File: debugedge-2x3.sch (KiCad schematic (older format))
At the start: 2 parts, among them J1 Conn_ARM_JTAG_SWD_10, J2 DebugEdge_02x03

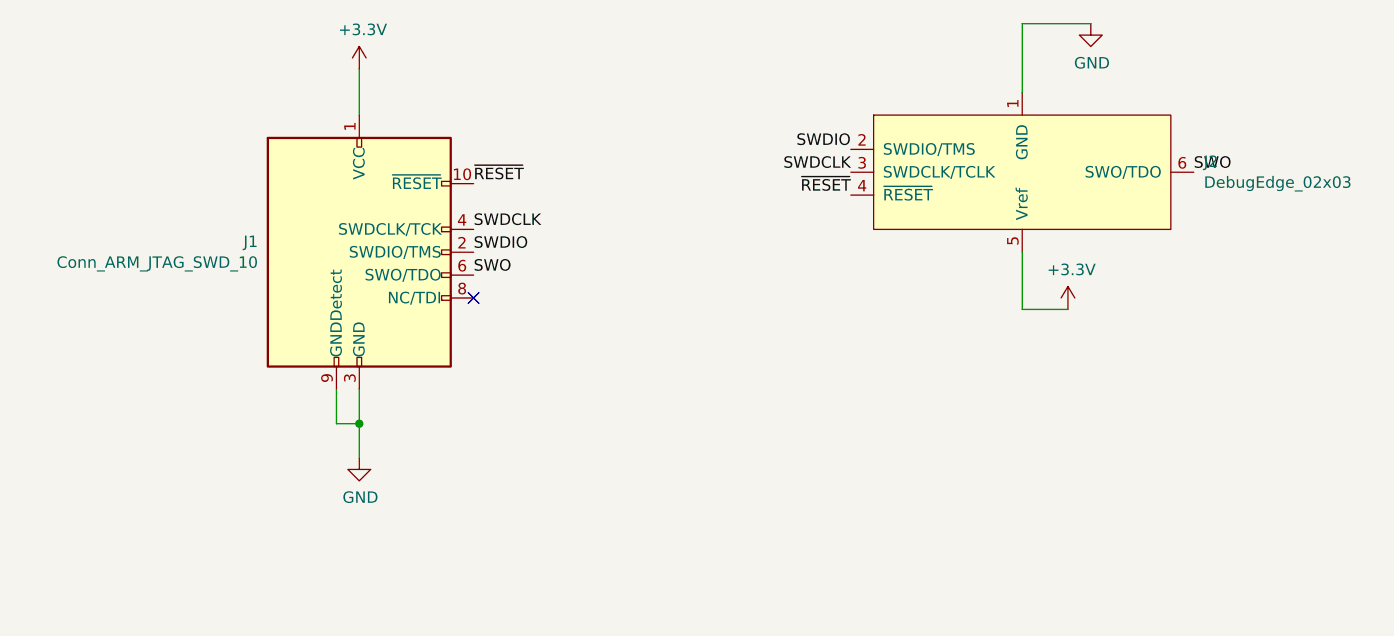
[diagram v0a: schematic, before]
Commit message: fix wrong connector
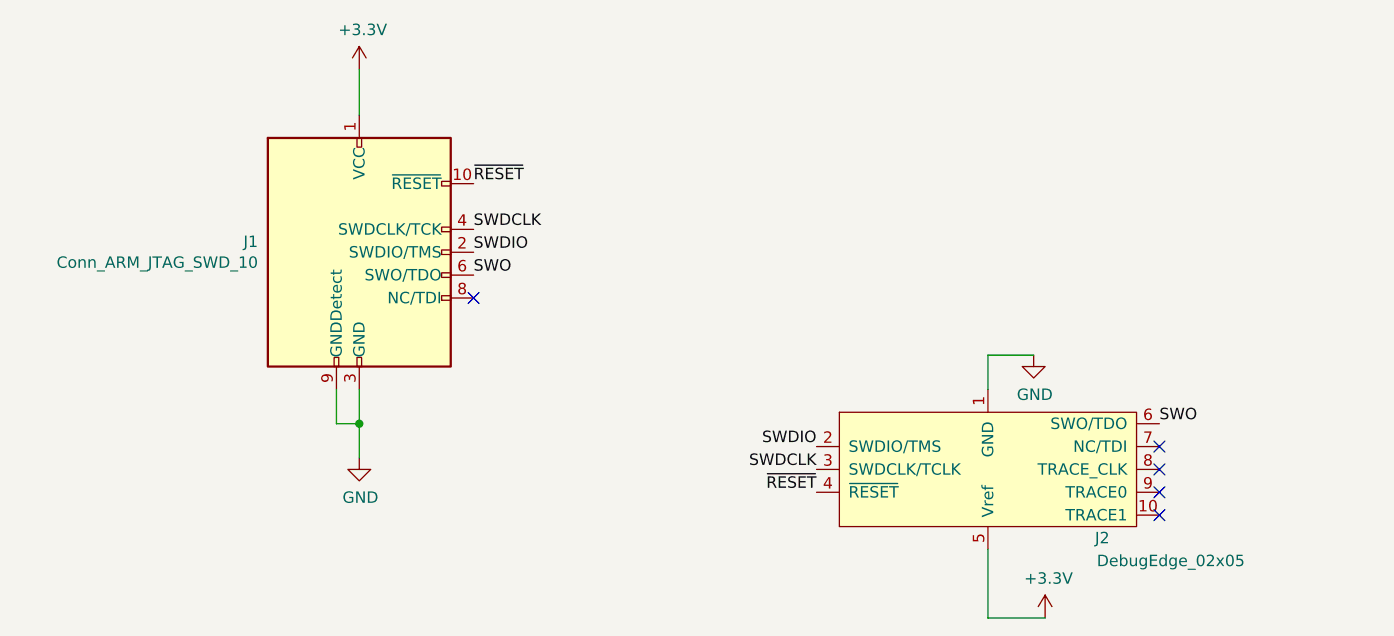
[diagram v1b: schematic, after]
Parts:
- removed J2: DebugEdge_02x03, Connector_DebugEdge:DebugEdge_2x03_Target, symbol Connector_DebugEdge:DebugEdge_02x03
- added J2: DebugEdge_02x05, Connector_DebugEdge:DebugEdge_2x05_Host, symbol Connector_DebugEdge:DebugEdge_02x05
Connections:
- net +3V3: now also J2.5 (Vref)
- net GND: now also J2.1 (GND)
- net SWDCLK: now also J2.3 (SWDCLK/TCLK)
- net SWDIO: now also J2.2 (SWDIO/TMS)
- net SWO: now also J2.6 (SWO/TDO)
- net ~RESET: now also J2.4 (~RESET~)
- no-connect marks 1 -> 5
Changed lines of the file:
@@
-$EndComp
-$Comp
-L Connector_DebugEdge:DebugEdge_02x03 J2
-U 1 1 5FF7E7FA
-P 5100 2450
-F 0 "J2" H 5894 2496 50  0000 L CNN
-F 1 "DebugEdge_02x03" H 5894 2405 50  0000 L CNN
-F 2 "Connector_DebugEdge:DebugEdge_2x03_Target" H 5100 2850 50  0001 C CNN
-F 3 "" H 5100 2850 50  0001 C CNN
-	1    5100 2450
-	1    0    0    -1
 $EndComp
 $Comp
 L power:GND #PWR0101
 U 1 1 5FF7F2E3
-P 5400 1800
-F 0 "#PWR0101" H 5400 1550 50  0001 C CNN
-F 1 "GND" H 5405 1627 50  0000 C CNN
-F 2 "" H 5400 1800 50  0001 C CNN
-F 3 "" H 5400 1800 50  0001 C CNN
-	1    5400 1800
+P 5150 3250
+F 0 "#PWR0101" H 5150 3000 50  0001 C CNN
+F 1 "GND" H 5155 3077 50  0000 C CNN
+F 2 "" H 5150 3250 50  0001 C CNN
+F 3 "" H 5150 3250 50  0001 C CNN
+	1    5150 3250
 	1    0    0    -1
 $EndComp
-Wire Wire Line
-	5400 1800 5100 1800
-Wire Wire Line
-	5100 1800 5100 2100
 $Comp
 L power:GND #PWR0102
@@
 L power:+3.3V #PWR0104
 U 1 1 5FF806B5
-P 5300 3050
-F 0 "#PWR0104" H 5300 2900 50  0001 C CNN
-F 1 "+3.3V" H 5315 3223 50  0000 C CNN
-F 2 "" H 5300 3050 50  0001 C CNN
-F 3 "" H 5300 3050 50  0001 C CNN
-	1    5300 3050
+P 5200 4400
+F 0 "#PWR0104" H 5200 4250 50  0001 C CNN
+F 1 "+3.3V" H 5215 4573 50  0000 C CNN
+F 2 "" H 5200 4400 50  0001 C CNN
+F 3 "" H 5200 4400 50  0001 C CNN
+	1    5200 4400
 	1    0    0    -1
 $EndComp
-Wire Wire Line
-	5300 3050 5100 3050
-Wire Wire Line
-	5100 3050 5100 2800
 Text Label 2700 2500 0    50   ~ 0
 ~RESET
-Text Label 4350 2550 2    50   ~ 0
+Text Label 4200 3850 2    50   ~ 0
 ~RESET
-Text Label 4350 2350 2    50   ~ 0
+Text Label 4200 3650 2    50   ~ 0
 SWDIO
 Text Label 2700 2800 0    50   ~ 0
@@
 Text Label 2700 2900 0    50   ~ 0
 SWO
-Text Label 5850 2450 0    50   ~ 0
+Text Label 5700 3550 0    50   ~ 0
 SWO
-Text Label 4350 2450 2    50   ~ 0
+Text Label 4200 3750 2    50   ~ 0
 SWDCLK
 NoConn ~ 2700 3000
+$Comp
+L Connector_DebugEdge:DebugEdge_02x05 J2
+U 1 1 600DAF2F
+P 4950 3750
+F 0 "J2" H 5450 3450 50  0000 C CNN
+F 1 "DebugEdge_02x05" H 5750 3350 50  0000 C CNN
+F 2 "Connector_DebugEdge:DebugEdge_2x05_Host" H 4950 4150 50  0001 C CNN
+F 3 "" H 4950 4150 50  0001 C CNN
+	1    4950 3750
+	1    0    0    -1
+$EndComp
+NoConn ~ 5700 3650
+NoConn ~ 5700 3750
+NoConn ~ 5700 3850
+NoConn ~ 5700 3950
+Wire Wire Line
+	4950 4100 4950 4400
+Wire Wire Line
+	4950 4400 5200 4400
+Wire Wire Line
+	5150 3250 4950 3250
+Wire Wire Line
+	4950 3250 4950 3400
 $EndSCHEMATC
